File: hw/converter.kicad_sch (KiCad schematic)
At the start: 18 parts, among them J301 1935776, J302 1935776, Q301 SW_L, Q302 SW_H

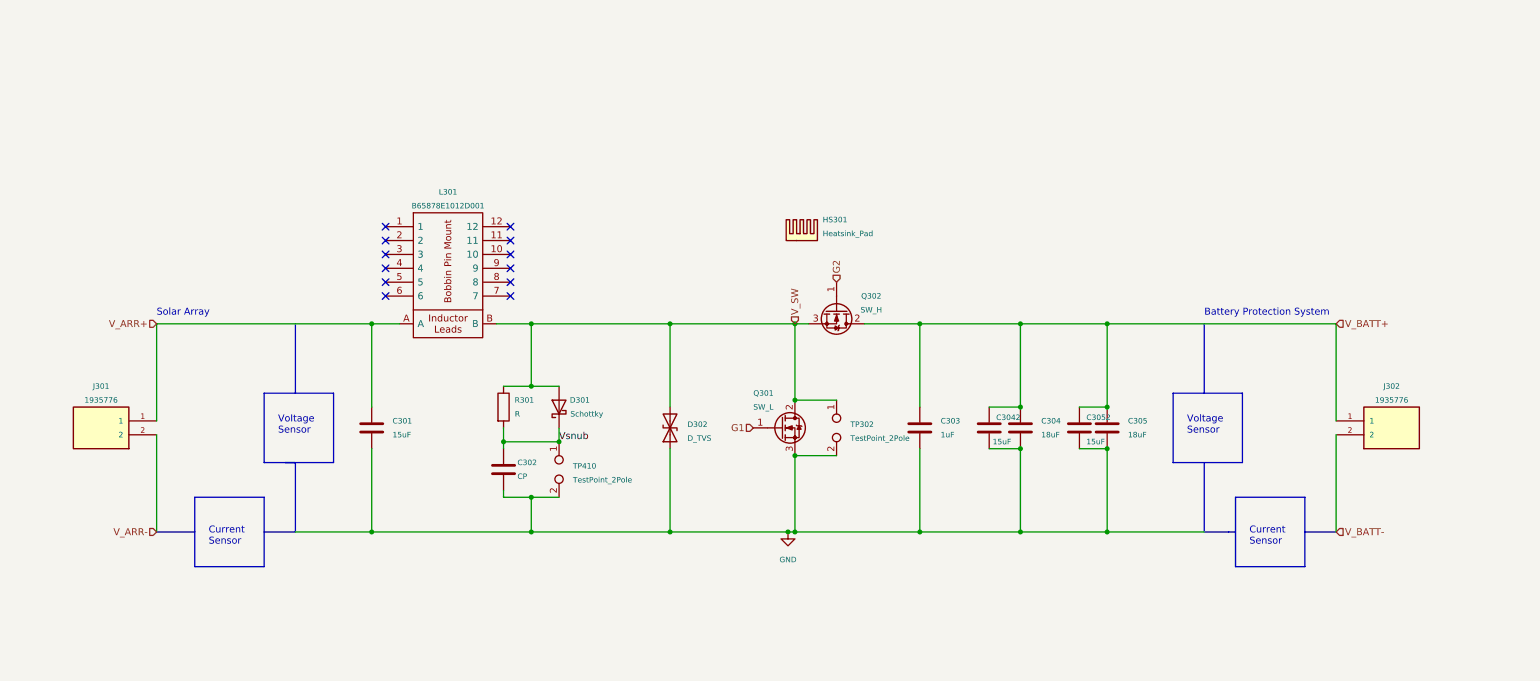
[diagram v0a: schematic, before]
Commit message: fixes for v0.1.1rc
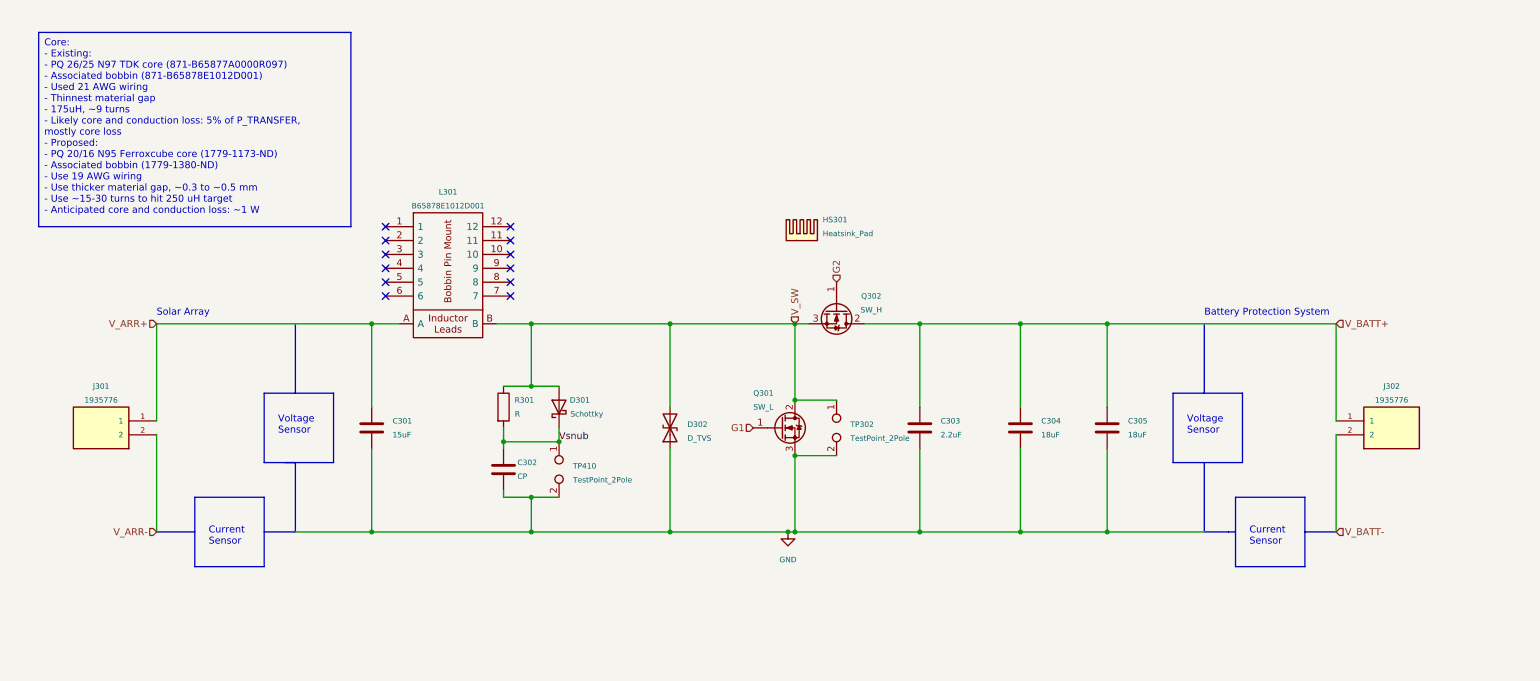
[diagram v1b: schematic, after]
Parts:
- removed C3042, C3052: 15uF, Capacitor_THT:C_Radial_D8.0mm_H11.5mm_P3.50mm, symbol Device:C
- C303: value 1uF -> 2.2uF
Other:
- company: (none) -> UT LHR Solar
- title: MPPT -> Sunscatter MPPT
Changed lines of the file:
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@@
   (paper "A4")
   (title_block
-    (title "MPPT")
-    (date "2023-01-30")
-    (rev "v0.0.0")
-    (comment 1 "Nishant Gupta")
+    (title "Sunscatter MPPT")
+    (date "2023-03-26")
+    (rev "v0.1.1")
+    (company "UT LHR Solar")
+    (comment 1 "Matthew Yu")
     (comment 2 "Jacob Pustilnik")
   )
@@
   (junction (at 214.63 71.12) (diameter 0) (color 0 0 0 0)
   )
-  (junction (at 214.63 93.98) (diameter 0) (color 0 0 0 0)
-  )
   (junction (at 157.48 71.12) (diameter 0) (color 0 0 0 0)
   )
@@
   (junction (at 109.22 109.22) (diameter 0) (color 0 0 0 0)
   )
-  (junction (at 198.755 93.98) (diameter 0) (color 0 0 0 0)
-  )
   (junction (at 80.01 109.22) (diameter 0) (color 0 0 0 0)
   )
@@
   (junction (at 157.48 85.09) (diameter 0) (color 0 0 0 0)
   )
-  (junction (at 198.755 86.36) (diameter 0) (color 0 0 0 0)
-  )
   (junction (at 180.34 71.12) (diameter 0) (color 0 0 0 0)
   )
@@
   )
   (junction (at 157.48 95.25) (diameter 0) (color 0 0 0 0)
-  )
-  (junction (at 214.63 86.36) (diameter 0) (color 0 0 0 0)
   )
   (junction (at 157.48 109.22) (diameter 0) (color 0 0 0 0)
@@
     (stroke (width 0) (type default))
   )
-  (wire (pts (xy 209.55 93.98) (xy 214.63 93.98))
-    (stroke (width 0) (type default))
-  )
   (wire (pts (xy 157.48 95.25) (xy 157.48 109.22))
     (stroke (width 0) (type default))
@@
     (stroke (width 0) (type default))
   )
-  (wire (pts (xy 193.04 93.98) (xy 198.755 93.98))
-    (stroke (width 0) (type default))
-  )
   (polyline (pts (xy 238.125 102.87) (xy 250.825 102.87))
     (stroke (width 0) (type default))
@@
     (stroke (width 0) (type default))
   )
-  (wire (pts (xy 193.04 86.36) (xy 198.755 86.36))
-    (stroke (width 0) (type default))
-  )
   (wire (pts (xy 104.14 82.55) (xy 109.22 82.55))
     (stroke (width 0) (type default))
@@
     (stroke (width 0) (type default))
   )
-  (wire (pts (xy 209.55 86.36) (xy 214.63 86.36))
-    (stroke (width 0) (type default))
-  )
   (wire (pts (xy 109.22 82.55) (xy 114.3 82.55))
     (stroke (width 0) (type default))
@@
   (wire (pts (xy 256.54 71.12) (xy 256.54 88.9))
     (stroke (width 0) (type default))
+  )
+  (text_box "Core:\n- Existing: \n  - PQ 26/25 N97 TDK core (871-B65877A0000R097)\n  - Associated bobbin (871-B65878E1012D001)\n  - Used 21 AWG wiring\n  - Thinnest material gap\n  - 175uH, ~9 turns\n  - Likely core and conduction loss: 5% of P_TRANSFER, mostly core loss\n- Proposed:\n  - PQ 20/16 N95 Ferroxcube core (1779-1173-ND)\n  - Associated bobbin (1779-1380-ND)\n  - Use 19 AWG wiring\n  - Use thicker material gap, ~0.3 to ~0.5 mm\n  - Use ~15-30 turns to hit 250 uH target\n  - Anticipated core and conduction loss: ~1 W"
+    (at 19.05 17.78 0) (size 57.15 35.56)
+    (stroke (width 0) (type default))
+    (fill (type none))
+    (effects (font (size 1.27 1.27)) (justify left top))
   )
   (text "Battery Protection System\n" (at 232.41 69.85 0)
@@
     )
   )
-  (symbol (lib_id "Device:C") (at 209.55 90.17 0) (unit 1)
-    (in_bom yes) (on_board yes) (dnp no)
-    (property "Reference" "C3052" (at 210.82 88.265 0)
-      (effects (font (size 1 1)) (justify left))
-    )
-    (property "Value" "15uF" (at 210.82 92.71 0)
-      (effects (font (size 1 1)) (justify left))
-    )
-    (property "Footprint" "Capacitor_THT:C_Radial_D8.0mm_H11.5mm_P3.50mm" (at 210.5152 93.98 0)
-      (effects (font (size 1.27 1.27)) hide)
-    )
-    (property "Datasheet" "https://www.mouser.com/datasheet/2/212/KEM_A4072_A759-1104329.pdf" (at 209.55 90.17 0)
-      (effects (font (size 1.27 1.27)) hide)
-    )
-    (property "Distributor" "Mouser" (at 209.55 90.17 0)
-      (effects (font (size 1.27 1.27)) hide)
-    )
-    (property "JLC P/N" "" (at 209.55 90.17 0)
-      (effects (font (size 1.27 1.27)) hide)
-    )
-    (property "Manufacturer" "KEMET" (at 209.55 90.17 0)
-      (effects (font (size 1.27 1.27)) hide)
-    )
-    (property "P/N" "80-A759KS156M2AAAE52" (at 209.55 90.17 0)
-      (effects (font (size 1.27 1.27)) hide)
-    )
-    (property "LCSC Part #" "" (at 209.55 90.17 0)
-      (effects (font (size 1.27 1.27)) hide)
-    )
-    (pin "1")
-    (pin "2")
-    (instances
-      (project "mppt"
-        (path "/06fd3a42-664d-41bc-bf0f-b5ee0ddcc902/9cd55a57-0ec8-481d-b571-b5fdbe353ce7"
-          (reference "C3052") (unit 1)
-        )
-      )
-    )
-  )
   (symbol (lib_id "Device:D_Schottky") (at 114.3 86.36 90) (unit 1)
     (in_bom yes) (on_board yes) (dnp no)
@@
       (effects (font (size 1 1)) (justify left))
     )
-    (property "Value" "1uF" (at 184.15 91.4399 0)
+    (property "Value" "2.2uF" (at 184.15 91.4399 0)
       (effects (font (size 1 1)) (justify left))
     )
@@
         )
       )
-    )
-  )
-  (symbol (lib_id "Device:C") (at 193.04 90.17 0) (unit 1)
-    (in_bom yes) (on_board yes) (dnp no)
-    (property "Reference" "C3042" (at 194.31 88.265 0)
-      (effects (font (size 1 1)) (justify left))
-    )
-    (property "Value" "15uF" (at 193.675 92.71 0)
-      (effects (font (size 1 1)) (justify left))
-    )
-    (property "Footprint" "Capacitor_THT:C_Radial_D8.0mm_H11.5mm_P3.50mm" (at 194.0052 93.98 0)
-      (effects (font (size 1.27 1.27)) hide)
-    )
-    (property "Datasheet" "https://www.mouser.com/datasheet/2/212/KEM_A4072_A759-1104329.pdf" (at 193.04 90.17 0)
-      (effects (font (size 1.27 1.27)) hide)
-    )
-    (property "Distributor" "Mouser" (at 193.04 90.17 0)
-      (effects (font (size 1.27 1.27)) hide)
-    )
-    (property "JLC P/N" "" (at 193.04 90.17 0)
-      (effects (font (size 1.27 1.27)) hide)
-    )
-    (property "Manufacturer" "KEMET" (at 193.04 90.17 0)
-      (effects (font (size 1.27 1.27)) hide)
-    )
-    (property "P/N" "80-A759KS156M2AAAE52" (at 193.04 90.17 0)
-      (effects (font (size 1.27 1.27)) hide)
-    )
-    (property "LCSC Part #" "" (at 193.04 90.17 0)
-      (effects (font (size 1.27 1.27)) hide)
-    )
-    (pin "1")
-    (pin "2")
-    (instances
-      (project "mppt"
-        (path "/06fd3a42-664d-41bc-bf0f-b5ee0ddcc902/9cd55a57-0ec8-481d-b571-b5fdbe353ce7"
-          (reference "C3042") (unit 1)
-        )
-      )

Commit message: updated instructions for v0.2.0 - v0.5.0 development candidates.
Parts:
- C301: Cost (none) -> 1.71
- C303: Cost (none) -> 3.26
- C304, C305: Cost (none) -> 2.58
- D302: Cost (none) -> 2.35
- J301, J302: Cost (none) -> 0.59
- L301: Cost (none) -> 9.04
- Q301, Q302: Cost (none) -> 6.25
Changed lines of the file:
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@@
   (title_block
     (title "Sunscatter MPPT")
-    (date "2023-03-26")
-    (rev "v0.1.1")
+    (date "2023-04-18")
+    (rev "v0.1.1rc")
     (company "UT LHR Solar")
     (comment 1 "Matthew Yu")
@@
       (effects (font (size 1.27 1.27)) hide)
     )
-    (property "JLC P/N" "" (at 40.64 88.9 0)
-      (effects (font (size 1.27 1.27)) hide)
-    )
     (property "Manufacturer" "Phoenix Contact" (at 40.64 88.9 0)
       (effects (font (size 1.27 1.27)) hide)
@@
       (effects (font (size 1.27 1.27)) hide)
     )
+    (property "Cost" "0.59" (at 40.64 88.9 0)
+      (effects (font (size 1.27 1.27)) hide)
+    )
     (pin "1")
     (pin "2")
@@
       (effects (font (size 1.27 1.27)) hide)
     )
-    (property "JLC P/N" "" (at 154.94 90.17 0)
-      (effects (font (size 1.27 1.27)) hide)
-    )
     (property "Manufacturer" "EPC" (at 154.94 90.17 0)
       (effects (font (size 1.27 1.27)) hide)
@@
     )
     (property "LCSC Part #" "" (at 154.94 90.17 0)
+      (effects (font (size 1.27 1.27)) hide)
+    )
+    (property "Cost" "6.25" (at 154.94 90.17 0)
       (effects (font (size 1.27 1.27)) hide)
     )
@@
       (effects (font (size 1.27 1.27)) hide)
     )
-    (property "JLC P/N" "" (at 256.54 88.9 0)
-      (effects (font (size 1.27 1.27)) hide)
-    )
     (property "Manufacturer" "Phoenix Contact" (at 256.54 88.9 0)
       (effects (font (size 1.27 1.27)) hide)
@@
     )
     (property "LCSC Part #" "" (at 256.54 88.9 0)
+      (effects (font (size 1.27 1.27)) hide)
+    )
+    (property "Cost" "0.59" (at 256.54 88.9 0)
       (effects (font (size 1.27 1.27)) hide)
     )
@@
       (effects (font (size 1.27 1.27)) hide)
     )
+    (property "Cost" "2.35" (at 134.62 90.17 0)
+      (effects (font (size 1.27 1.27)) hide)
+    )
     (pin "1")
     (pin "2")
@@
     )
     (property "LCSC Part #" "" (at 114.3 86.36 0)
+      (effects (font (size 1.27 1.27)) hide)
+    )
+    (property "Cost" "" (at 114.3 86.36 0)
       (effects (font (size 1.27 1.27)) hide)
     )
@@
       (effects (font (size 1.27 1.27)) hide)
     )
-    (property "JLC P/N" "" (at 180.34 90.17 0)
-      (effects (font (size 1.27 1.27)) hide)
-    )
     (property "Manufacturer" "TDK" (at 180.34 90.17 0)
       (effects (font (size 1.27 1.27)) hide)
@@
       (effects (font (size 1.27 1.27)) hide)
     )
+    (property "Cost" "3.26" (at 180.34 90.17 0)
+      (effects (font (size 1.27 1.27)) hide)
+    )
     (pin "1")
     (pin "2")
@@
       (effects (font (size 1.27 1.27)) hide)
     )
-    (property "JLC P/N" "" (at 165.1 68.58 0)
-      (effects (font (size 1.27 1.27)) hide)
-    )
     (property "Manufacturer" "EPC" (at 165.1 68.58 0)
       (effects (font (size 1.27 1.27)) hide)
@@
     )
     (property "LCSC Part #" "" (at 165.1 68.58 0)
+      (effects (font (size 1.27 1.27)) hide)
+    )
+    (property "Cost" "6.25" (at 165.1 68.58 0)
       (effects (font (size 1.27 1.27)) hide)
     )
@@
       (effects (font (size 1.27 1.27)) hide)
     )
+    (property "Cost" "" (at 114.3 97.79 0)
+      (effects (font (size 1.27 1.27)) hide)
+    )
     (pin "1")
     (pin "2")
@@
       (effects (font (size 1.27 1.27)) hide)
     )
+    (property "Cost" "" (at 165.1 90.17 0)
+      (effects (font (size 1.27 1.27)) hide)
+    )
     (pin "1")
     (pin "2")
@@
     )
     (property "LCSC Part #" "" (at 104.14 97.79 0)
+      (effects (font (size 1.27 1.27)) hide)
+    )
+    (property "Cost" "" (at 104.14 97.79 0)
       (effects (font (size 1.27 1.27)) hide)
     )
@@
       (effects (font (size 1.27 1.27)) hide)
     )
-    (property "JLC P/N" "" (at 80.01 90.17 0)
-      (effects (font (size 1.27 1.27)) hide)
-    )
     (property "Manufacturer" "KEMET" (at 80.01 90.17 0)
       (effects (font (size 1.27 1.27)) hide)
@@
       (effects (font (size 1.27 1.27)) hide)
     )
+    (property "Cost" "1.71" (at 80.01 90.17 0)
+      (effects (font (size 1.27 1.27)) hide)
+    )
     (pin "1")
     (pin "2")
@@
       (effects (font (size 1.27 1.27)) hide)
     )
-    (property "JLC P/N" "" (at 158.75 55.88 0)
-      (effects (font (size 1.27 1.27)) hide)
-    )
     (property "Manufacturer" "WayInTop" (at 158.75 55.88 0)
       (effects (font (size 1.27 1.27)) hide)
@@
     )
     (property "LCSC Part #" "" (at 158.75 55.88 0)
+      (effects (font (size 1.27 1.27)) hide)
+    )
+    (property "Cost" "" (at 158.75 55.88 0)
       (effects (font (size 1.27 1.27)) hide)
     )
@@
     )
     (property "LCSC Part #" "" (at 104.14 86.36 0)
+      (effects (font (size 1.27 1.27)) hide)
+    )
+    (property "Cost" "" (at 104.14 86.36 0)
       (effects (font (size 1.27 1.27)) hide)
     )
@@
       (effects (font (size 1.27 1.27)) hide)
     )
-    (property "JLC P/N" "" (at 198.755 90.17 0)
-      (effects (font (size 1.27 1.27)) hide)
-    )
     (property "Manufacturer" "KEMET" (at 198.755 90.17 0)
       (effects (font (size 1.27 1.27)) hide)
@@
       (effects (font (size 1.27 1.27)) hide)
     )
+    (property "Cost" "2.58" (at 198.755 90.17 0)
+      (effects (font (size 1.27 1.27)) hide)
+    )
     (pin "1")
     (pin "2")
@@
       (effects (font (size 1.27 1.27)) hide)
     )
-    (property "JLC P/N" "" (at 214.63 90.17 0)
-      (effects (font (size 1.27 1.27)) hide)
-    )
     (property "Manufacturer" "KEMET" (at 214.63 90.17 0)
       (effects (font (size 1.27 1.27)) hide)
@@
     )
     (property "LCSC Part #" "" (at 214.63 90.17 0)
+      (effects (font (size 1.27 1.27)) hide)
+    )
+    (property "Cost" "2.58" (at 214.63 90.17 0)
       (effects (font (size 1.27 1.27)) hide)
     )
@@
       (effects (font (size 1.27 1.27)) hide)
     )
-    (property "JLC P/N" "" (at 82.55 53.34 0)
-      (effects (font (size 1.27 1.27)) hide)
-    )
     (property "Manufacturer" "EPCOS/TDK" (at 82.55 53.34 0)
       (effects (font (size 1.27 1.27)) hide)
@@
       (effects (font (size 1.27 1.27)) hide)
     )
+    (property "Cost" "9.04" (at 82.55 53.34 0)
+      (effects (font (size 1.27 1.27)) hide)
+    )
